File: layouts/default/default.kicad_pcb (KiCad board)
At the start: 2 copper layers, 27.8 x 14.2 mm, 16 parts

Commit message: finalish layout
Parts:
- moved MIC1 5.99 mm to (84.2, 61.5), turned to -90 degrees
- moved C1 1.33 mm to (82.5, 63.9)
- moved U2 1.33 mm to (85.0, 63.9)
- moved R1 1.33 mm to (86.2, 65.6)
- moved C2 1.33 mm to (84.3, 65.6)
- moved R2 0.19 mm to (88.5, 59.8)
- moved R3 0.19 mm to (84.0, 59.8)
- moved U1 0.19 mm to (86.4, 56.1)
- moved C4 0.18 mm to (73.3, 55.1)
- moved R5 0.18 mm to (76.7, 57.4)
- moved C3 0.18 mm to (77.9, 57.4)
- moved C5 0.18 mm to (78.1, 62.5)
- moved L2 0.18 mm to (74.9, 62.3)
- moved R4 0.18 mm to (75.9, 55.3)
- moved U3 0.18 mm to (74.4, 58.0)
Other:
- board size 27.8 x 14.2 mm -> 27.5 x 14.2 mm

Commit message: meow
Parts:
- added U4: , atopile:LGA-14_L3.0-W2.5-P0.50-TL-eab322, F.Cu at (89.2, 62.4)
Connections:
- net DP2 renamed A6
- C1 pad 1: hv-1 -> hv
- C1 pad 2: gnd-1 -> gnd
- C2 pad 1: hv-2 -> hv-1
- C2 pad 2: gnd-1 -> gnd
- C3 pad 1: hv -> VCC
- C4 pad 1: VIN -> hv-1
- C5 pad 1: hv -> VCC
- L1 pad 1: GND -> gnd
- L1 pad 11: GND -> gnd
- L1 pad 12: uc-net-12 -> uc-net-8
- L1 pad 13: uc-net-7 -> uc-net-11
- L1 pad 14: GND -> gnd
- L1 pad 18: uc-net -> uc-net-10
- L1 pad 19: uc-net-1 -> uc-net-15
- L1 pad 2: GND -> gnd
- L1 pad 22: uc-net-2 -> uc-net-14
- L1 pad 23: uc-net-4 -> uc-net-7
- L1 pad 24: uc-net-5 -> uc-net-2
- L1 pad 26: uc-net-15 -> uc-net-1
- L1 pad 27: uc-net-8 -> uc-net-9
- L1 pad 28: uc-net-11 -> uc-net-13
- L1 pad 29: uc-net-6 -> uc-net-16
- L1 pad 3: uc-VCC -> VCC
- L1 pad 30: uc-net-16 -> uc-line
- L1 pad 31: uc-net-10 -> uc-line-1
- L1 pad 32: uc-net-17 -> uc-net-6
- L1 pad 33: uc-net-13 -> uc-net-4
- L1 pad 36: GND -> gnd
- L1 pad 37: GND -> gnd
- L1 pad 38: GND -> gnd
- L1 pad 39: GND -> gnd
- L1 pad 40: GND -> gnd
- L1 pad 41: GND -> gnd
- L1 pad 42: GND -> gnd
- L1 pad 43: GND -> gnd
- L1 pad 44: GND -> gnd
- L1 pad 45: GND -> gnd
- L1 pad 46: GND -> gnd
- L1 pad 47: GND -> gnd
- L1 pad 48: GND -> gnd
- L1 pad 49: GND -> gnd
- L1 pad 5: uc-net-14 -> uc-net-5
- L1 pad 50: GND -> gnd
- L1 pad 51: GND -> gnd
- L1 pad 52: GND -> gnd
- L1 pad 53: GND -> gnd
- L1 pad 54: GND -> gnd
- L1 pad 55: GND -> gnd
- L1 pad 56: GND -> gnd
- L1 pad 57: GND -> gnd
- L1 pad 58: GND -> gnd
- L1 pad 59: GND -> gnd
- L1 pad 6: uc-net-18 -> uc-net
- L1 pad 60: GND -> gnd
- L1 pad 61: GND -> gnd
- L1 pad 8: uc-net-9 -> uc-net-12
- L2 pad 2: hv -> VCC
- MIC1 pad 2: gnd-2 -> gnd
- MIC1 pad 3: gnd-2 -> gnd
- R1 pad 2: gnd-1 -> gnd
- R2 pad 2: usb-gnd -> gnd
- R3 pad 2: usb-gnd -> gnd
- R5 pad 1: hv -> VCC
- U1 pad 1: usb-gnd -> gnd
- U1 pad 2: usb-gnd -> gnd
- U1 pad 3: usb-gnd -> gnd
- U1 pad 4: usb-gnd -> gnd
- U1 pad A1: usb-gnd -> gnd
- U1 pad A12: usb-gnd -> gnd
- U1 pad A4: VBUS -> hv
- U1 pad A9: VBUS -> hv
- U1 pad B1: usb-gnd -> gnd
- U1 pad B12: usb-gnd -> gnd
- U1 pad B4: VBUS -> hv
- U1 pad B9: VBUS -> hv
- U2 pad 1: hv-1 -> hv
- U2 pad 10: hv-2 -> hv-1
- U2 pad 11: gnd-1 -> gnd
- U2 pad 3: gnd-1 -> gnd
- U2 pad 7: hv-1 -> hv
- U3 pad 4: VIN -> hv-1
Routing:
- net VCC: track 0.00 -> 8.24 mm
- net hv-1: track 6.74 -> 2.99 mm, vias 2 -> 0
- net gnd-1: track 3.06 -> 0.00 mm
- net gnd: track 7.54 -> 10.6 mm
- net VIN: track 1.83 -> 0.00 mm
- net hv: track 8.24 -> 6.74 mm, vias 0 -> 2
- net hv-2: track 1.16 -> 0.00 mm

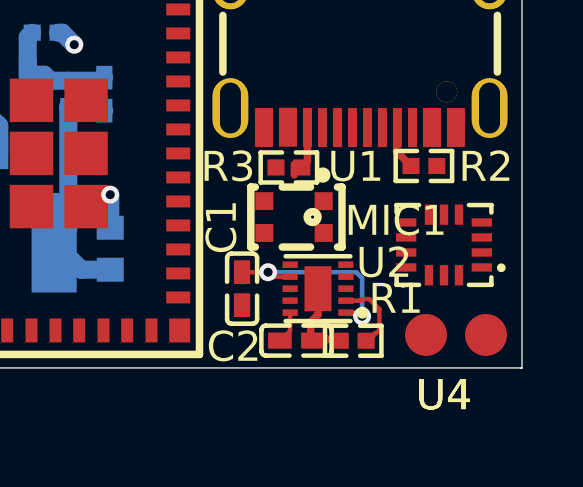
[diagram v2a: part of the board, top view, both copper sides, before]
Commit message: removed acc, fixed ldo (implement in main ncp release)
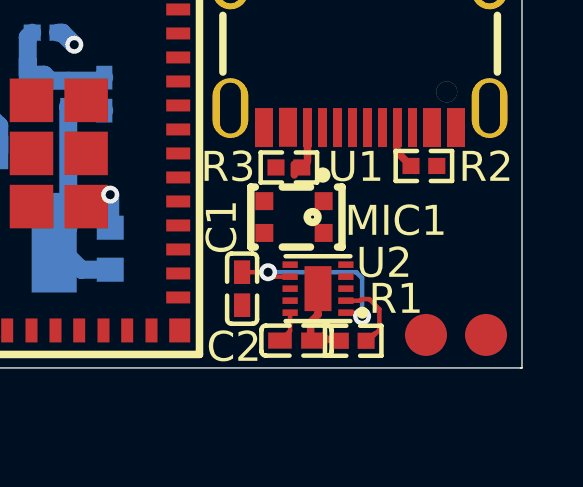
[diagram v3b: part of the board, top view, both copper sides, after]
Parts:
- removed U4: , atopile:LGA-14_L3.0-W2.5-P0.50-TL-eab322
- R2, R3: value 4.7kΩ ±1% 62.5mW -> 5.1kΩ ±1% 62.5mW
- R5: value 100kΩ ±1% 62.5mW -> 909kΩ ±1% 62.5mW
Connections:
- net A5 renamed CC1
- net A6 renamed DP1
- net B8 renamed SUB2
- net CC2 renamed B5
- net DN2 renamed DN1
- C1 pad 1: hv -> hv-1
- C2 pad 1: hv-1 -> hv
- C4 pad 1: hv-1 -> hv
- L1 pad 12: uc-net-8 -> uc-net-10
- L1 pad 13: uc-net-11 -> uc-net-9
- L1 pad 16: uc-net-3 -> uc-net-6
- L1 pad 18: uc-net-10 -> uc-net
- L1 pad 19: uc-net-15 -> uc-net-5
- L1 pad 23: uc-net-7 -> uc-net-2
- L1 pad 24: uc-net-2 -> uc-net-15
- L1 pad 26: uc-net-1 -> uc-net-13
- L1 pad 27: uc-net-9 -> uc-net-7
- L1 pad 28: uc-net-13 -> uc-net-1
- L1 pad 29: uc-net-16 -> uc-net-3
- L1 pad 32: uc-net-6 -> uc-net-16
- L1 pad 5: uc-net-5 -> uc-net-11
- L1 pad 6: uc-net -> uc-net-12
- L1 pad 8: uc-net-12 -> uc-net-8
- U1 pad A4: hv -> hv-1
- U1 pad A9: hv -> hv-1
- U1 pad B4: hv -> hv-1
- U1 pad B9: hv -> hv-1
- U2 pad 1: hv -> hv-1
- U2 pad 10: hv-1 -> hv
- U2 pad 7: hv -> hv-1
- U3 pad 4: hv-1 -> hv
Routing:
- net hv-1: track 2.99 -> 6.74 mm, vias 0 -> 2
- net hv: track 6.74 -> 2.99 mm, vias 2 -> 0

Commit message: updates
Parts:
- moved R1 4.56 mm to (90.3, 63.7)
- moved C2 4.56 mm to (88.4, 63.7)
- moved U2 4.56 mm to (89.1, 61.9)
- moved C1 4.53 mm to (86.6, 62.0)
- moved MIC1 0.76 mm to (83.6, 61.9)
- moved R2 0.35 mm to (88.4, 60.1)
- moved R3 0.33 mm to (84.0, 60.1)
- moved U1 0.33 mm to (86.4, 56.4)
- moved C3 0.18 mm to (78.0, 57.2)
- moved C4 0.18 mm to (73.4, 55.0)
- moved C5 0.18 mm to (78.2, 62.4)
- moved L2 0.18 mm to (75.0, 62.2)
- moved R4 0.18 mm to (76.0, 55.2)
- moved R5 0.18 mm to (76.8, 57.2)
- moved U3 0.18 mm to (74.5, 57.9)
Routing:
- net gnd: track 10.6 -> 39.0 mm, vias 2 -> 6
- net hv-1: track 6.74 -> 20.6 mm, vias 2 -> 3
- net VCC: track 8.24 -> 14.2 mm, vias 0 -> 1
- net EN: track 0.00 -> 3.27 mm, vias 0 -> 1

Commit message: almost done
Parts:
- added C6: 100nF ±10% 16V X7R, atopile:C0402-b3ef17, F.Cu at (81.6, 62.4)
- C1, C2: value 1µF ±10% 25V X5R -> 1µF ±10% 16V X5R
- MIC1: footprint atopile:MIC-SMD_4P-L2.8-W1.9-P1.84-TL-8e01f2 -> atopile:MIC-SMD_5P-L3.5-W2.7-TL_MMICT390200012-12501e
- R5: value 909kΩ ±1% 62.5mW -> 953kΩ ±1% 62.5mW
- moved R3 1.40 mm to (82.6, 60.1)
- moved MIC1 0.51 mm to (83.9, 62.4), turned to 90 degrees
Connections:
- net SUB2 renamed B8
- net uc-net renamed uc-line-2
- net uc-net-1 renamed uc-line-13
- net uc-net-11 renamed uc-line-5
- net uc-net-12 renamed uc-line-8
- net uc-net-14 renamed uc-line-11
- net uc-net-16 renamed uc-line-9
- net uc-net-2 renamed uc-line-3
- net uc-net-3 renamed uc-line-12
- net uc-net-4 renamed uc-line-4
- net uc-net-5 renamed uc-line-6
- net uc-net-7 renamed uc-line-7
- net uc-net-8 renamed uc-line-10
- C3 pad 1: VCC -> hv-2
- C5 pad 1: VCC -> hv-2
- L1 pad 12: uc-net-10 -> SELECT
- L1 pad 13: uc-net-9 -> DATA
- L1 pad 16: uc-net-6 -> CLK
- L1 pad 24: uc-net-15 -> uc-line
- L1 pad 26: uc-net-13 -> uc-line-1
- L1 pad 3: VCC -> hv-2
- L1 pad 30: uc-line -> line
- L1 pad 31: uc-line-1 -> line-1
- L2 pad 2: VCC -> hv-2
- MIC1 pad 1: OUT -> DATA
- MIC1 pad 2: gnd -> SELECT
- MIC1 pad 4: VCC -> CLK
- R5 pad 1: VCC -> hv-2
- U1 pad A6: DP1 -> line-1
- U1 pad A7: DN1 -> line
- U1 pad B6: DP1 -> line-1
- U1 pad B7: DN1 -> line
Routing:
- net hv: track 2.99 -> 25.0 mm, vias 0 -> 2
- net line-1: track 0.00 -> 20.0 mm, vias 0 -> 2
- net hv-2: track 0.00 -> 19.9 mm, vias 0 -> 2
- net line: track 0.00 -> 19.9 mm, vias 0 -> 2
- net VCC: track 14.2 -> 0.00 mm, vias 1 -> 0
- net gnd: track 39.0 -> 52.2 mm, vias 6 -> 11
- net SELECT: track 0.00 -> 3.59 mm
- net CLK: track 0.00 -> 3.56 mm
- net DATA: track 0.00 -> 2.57 mm
- net B5: track 1.44 -> 2.87 mm, vias 0 -> 1
- net CHG: vias 1 -> 0
- added copper zone on B.Cu, net gnd
- added copper zone on F.Cu, net gnd
- added copper zone on In1.Cu, net gnd
- added copper zone on In2.Cu, net gnd
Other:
- copper layers 2 -> 4

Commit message: eod
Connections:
- net B5 renamed CC2
- net B8 renamed SUB2
- net CC1 renamed A5
- net SUB1 renamed A8
- C2 pad 1: hv -> hv-2
- C3 pad 1: hv-2 -> hv
- C4 pad 1: hv -> hv-2
- C5 pad 1: hv-2 -> hv
- C6 pad 1: hv-2 -> hv
- L1 pad 18: uc-line-2 -> uc-line-7
- L1 pad 22: uc-line-11 -> uc-line-8
- L1 pad 23: uc-line-3 -> uc-line-9
- L1 pad 24: uc-line -> uc-line-12
- L1 pad 26: uc-line-1 -> uc-line-5
- L1 pad 27: uc-line-7 -> uc-line-4
- L1 pad 28: uc-line-13 -> uc-line-11
- L1 pad 29: uc-line-12 -> uc-line-1
- L1 pad 3: hv-2 -> hv
- L1 pad 32: uc-line-9 -> uc-line
- L1 pad 33: uc-line-4 -> uc-line-2
- L1 pad 5: uc-line-5 -> uc-line-3
- L1 pad 6: uc-line-8 -> uc-line-10
- L1 pad 8: uc-line-10 -> EN
- L2 pad 2: hv-2 -> hv
- MIC1 pad 5: hv-2 -> hv
- R5 pad 1: hv-2 -> hv
- U2 pad 10: hv -> hv-2
- U3 pad 4: hv -> hv-2
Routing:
- net hv: track 25.0 -> 19.3 mm
- net hv-2: track 19.9 -> 24.1 mm
- net gnd: track 52.2 -> 55.7 mm, vias 11 -> 12
- net line-1: track 20.0 -> 19.4 mm
- net hv-1: track 20.3 -> 19.7 mm
- net EN: track 3.27 -> 3.17 mm, vias 1 -> 0
- net (no net): vias 0 -> 1

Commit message: updates
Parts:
- added C7: 100nF ±10% 16V X7R, atopile:C0402-b3ef17, B.Cu at (73.6, 59.4)
- added C8: 100nF ±10% 16V X7R, atopile:C0402-b3ef17, B.Cu at (72.5, 64.0)
- added C9: 100nF ±10% 50V X7R, atopile:C0603-bd72f6, F.Cu at (0.00, 0.00)
- added U4: , atopile:LGA-14_L3.0-W2.5-P0.50-TL-eab322, B.Cu at (71.6, 60.2)
- moved C3 1.20 mm to (79.2, 57.4)
- moved L2 1.20 mm to (76.2, 62.1)
- moved R4 1.20 mm to (77.2, 55.1)
- moved C5 1.20 mm to (79.4, 62.3)
- moved R5 1.20 mm to (78.0, 57.2)
- moved U3 1.20 mm to (75.7, 57.8)
- moved C4 1.20 mm to (74.6, 54.9)
- moved C6 0.22 mm to (81.8, 62.4)
- moved MIC1 0.21 mm to (84.1, 62.4)
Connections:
- net A5 renamed CC1
- net CC2 renamed B5
- C1 pad 1: hv-1 -> hv
- C3 pad 1: hv -> hv-1
- C5 pad 1: hv -> hv-1
- C6 pad 1: hv -> hv-1
- L1 pad 18: uc-line-7 -> uc-line-5
- L1 pad 19: uc-line-6 -> uc-line-9
- L1 pad 22: uc-line-8 -> uc-line-3
- L1 pad 23: uc-line-9 -> uc-line-4
- L1 pad 24: uc-line-12 -> uc-line-2
- L1 pad 26: uc-line-5 -> uc-line-10
- L1 pad 27: uc-line-4 -> uc-line-8
- L1 pad 28: uc-line-11 -> uc-line
- L1 pad 3: hv -> hv-1
- L1 pad 32: uc-line -> SDA
- L1 pad 33: uc-line-2 -> SCL
- L1 pad 5: uc-line-3 -> uc-line-7
- L1 pad 6: uc-line-10 -> uc-line-6
- L2 pad 2: hv -> hv-1
- MIC1 pad 5: hv -> hv-1
- R5 pad 1: hv -> hv-1
- U1 pad A4: hv-1 -> hv
- U1 pad A9: hv-1 -> hv
- U1 pad B4: hv-1 -> hv
- U1 pad B9: hv-1 -> hv
- U2 pad 1: hv-1 -> hv
- U2 pad 7: hv-1 -> hv
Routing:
- net hv-1: track 19.7 -> 33.2 mm, vias 3 -> 2
- net gnd: track 55.7 -> 68.1 mm, vias 12 -> 14
- net SCL: track 0.00 -> 8.78 mm, vias 0 -> 1
- net SDA: track 0.00 -> 8.06 mm, vias 0 -> 1
- net hv: track 19.3 -> 24.2 mm, vias 2 -> 3
- net hv-2: track 24.1 -> 22.4 mm
- net uc.footprint.pins[12].net-net: vias 0 -> 1
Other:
- board text added: "3V3"
- board text added: "5V"
- board text added: "GND"
- board text added: "SCL"
- board text added: "SDA"

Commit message: updates
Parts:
- C9: moved to B.Cu
- moved C9 95.7 mm to (72.0, 63.1), turned to 180 degrees
- moved C8 0.72 mm to (73.2, 64.4)
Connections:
- C2 pad 1: hv-2 -> hv-1
- C3 pad 1: hv-1 -> hv-2
- C4 pad 1: hv-2 -> hv-1
- C5 pad 1: hv-1 -> hv-2
- C6 pad 1: hv-1 -> hv-2
- C7 pad 1: hv-1 -> hv-2
- C8 pad 1: hv-1 -> hv-2
- C9 pad 1: hv-1 -> hv-2
- L1 pad 18: uc-line-5 -> uc-line-1
- L1 pad 19: uc-line-9 -> uc-line-5
- L1 pad 22: uc-line-3 -> uc-line-7
- L1 pad 23: uc-line-4 -> uc-line-3
- L1 pad 24: uc-line-2 -> uc-line-6
- L1 pad 26: uc-line-10 -> uc-line-9
- L1 pad 27: uc-line-8 -> uc-line-4
- L1 pad 29: uc-line-1 -> uc-line-2
- L1 pad 3: hv-1 -> hv-2
- L1 pad 30: line -> line-1
- L1 pad 31: line-1 -> line
- L1 pad 5: uc-line-7 -> uc-line-8
- L1 pad 6: uc-line-6 -> uc-line-10
- L2 pad 2: hv-1 -> hv-2
- MIC1 pad 5: hv-1 -> hv-2
- R5 pad 1: hv-1 -> hv-2
- U1 pad A6: line-1 -> line
- U1 pad A7: line -> line-1
- U1 pad B6: line-1 -> line
- U1 pad B7: line -> line-1
- U2 pad 10: hv-2 -> hv-1
- U3 pad 4: hv-2 -> hv-1
- U4 pad 12: hv-1 -> hv-2
- U4 pad 5: hv-1 -> hv-2
- U4 pad 8: hv-1 -> hv-2
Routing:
- net hv-1: track 33.2 -> 22.4 mm
- net hv-2: track 22.4 -> 32.9 mm
- net gnd: track 68.1 -> 67.5 mm, vias 14 -> 15
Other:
- board text added: "+"
- board text added: "BAT"
